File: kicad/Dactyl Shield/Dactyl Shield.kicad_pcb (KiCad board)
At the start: 4 copper layers, 99.4 x 77.4 mm, 122 parts, among them J201 JST, J202 Split, J203 Column, J204 Thumb, J205 External, J206 Row, J207 Display, J208 Vic, J209 ResA, J212 ResB, J301 JST, J302 Split, J303 Column, J304 Thumb, J305 External, J306 Row, J307 Display, J308 Vic, J309 ResA, J312 ResB, Q201 AO3400A, Q301 AO3400A, SW201 Battery, SW202 Reset, SW203 LED, SW301 Battery, SW302 Reset, SW303 LED, U201 SRV05-4, U202 Nice!Nano/2040, U301 SRV05-4, U302 Nice!Nano/2040

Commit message: refactor: cleanup schematic; external -> foot
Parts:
- J205, J305: value External -> Foot
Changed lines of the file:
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@@
 			)
 		)
-		(property "Value" "External"
-			(at 0.9 -2.1 90)
+		(property "Value" "Foot"
+			(at 0.25 -2.1 90)
 			(layer "F.SilkS")
 			(effects
@@
 		(fp_arc
 			(start 6.938123 15.132041)
-			(mid 6.337066 14.8831)
+			(mid 6.337062 14.8831)
 			(end 6.088123 14.282041)
 			(stroke
@@
 		(fp_arc
 			(start 8.236041 -15.740877)
-			(mid 8.837089 -15.491924)
+			(mid 8.837086 -15.491923)
 			(end 9.086041 -14.890877)
 			(stroke
@@
 		(fp_arc
 			(start 6.938123 15.132041)
-			(mid 6.337066 14.8831)
+			(mid 6.337062 14.8831)
 			(end 6.088123 14.282041)
 			(stroke
@@
 		(fp_arc
 			(start 8.236041 -15.740877)
-			(mid 8.837089 -15.491924)
+			(mid 8.837086 -15.491923)
 			(end 9.086041 -14.890877)
 			(stroke
@@
 			)
 		)
-		(property "Value" "External"
-			(at -0.9 -2 90)
+		(property "Value" "Foot"
+			(at -0.35 -2 90)
 			(layer "F.SilkS")
 			(effects

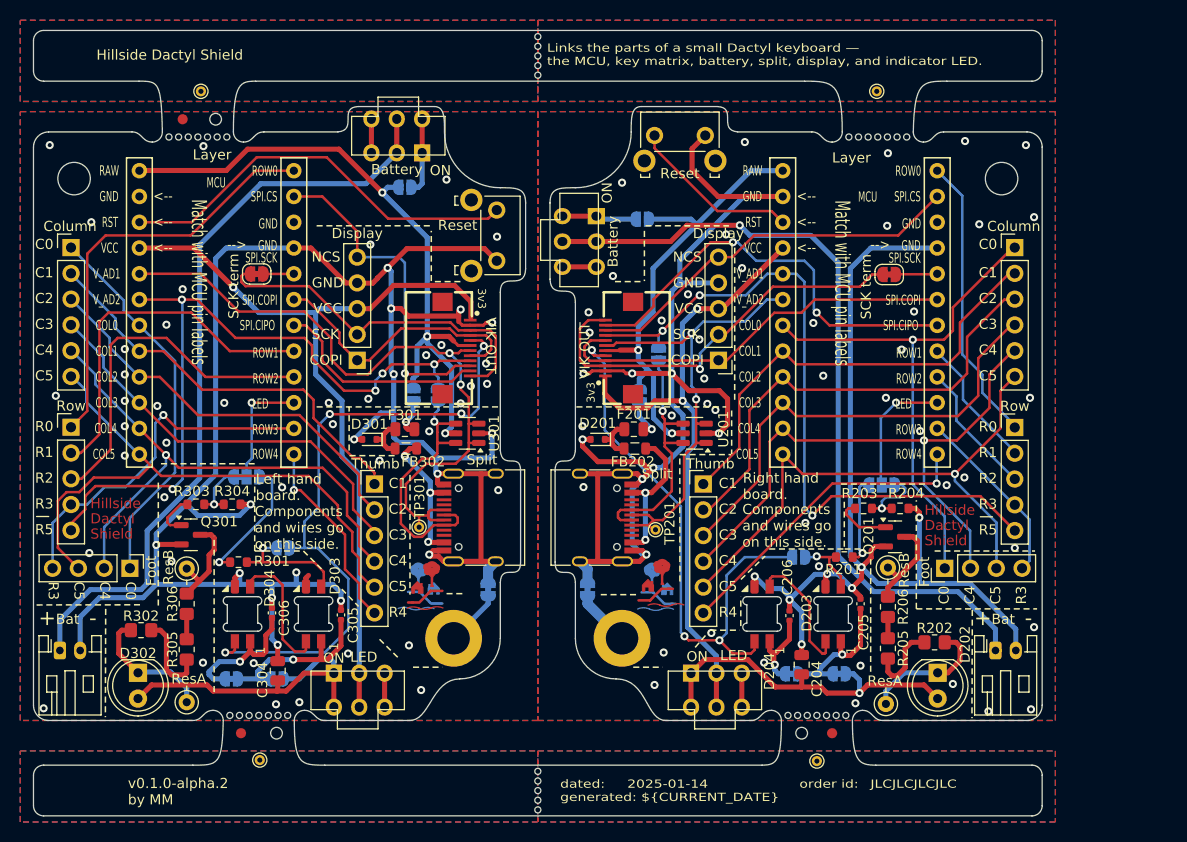
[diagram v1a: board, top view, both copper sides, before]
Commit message: feat: reset on back, power slides to right
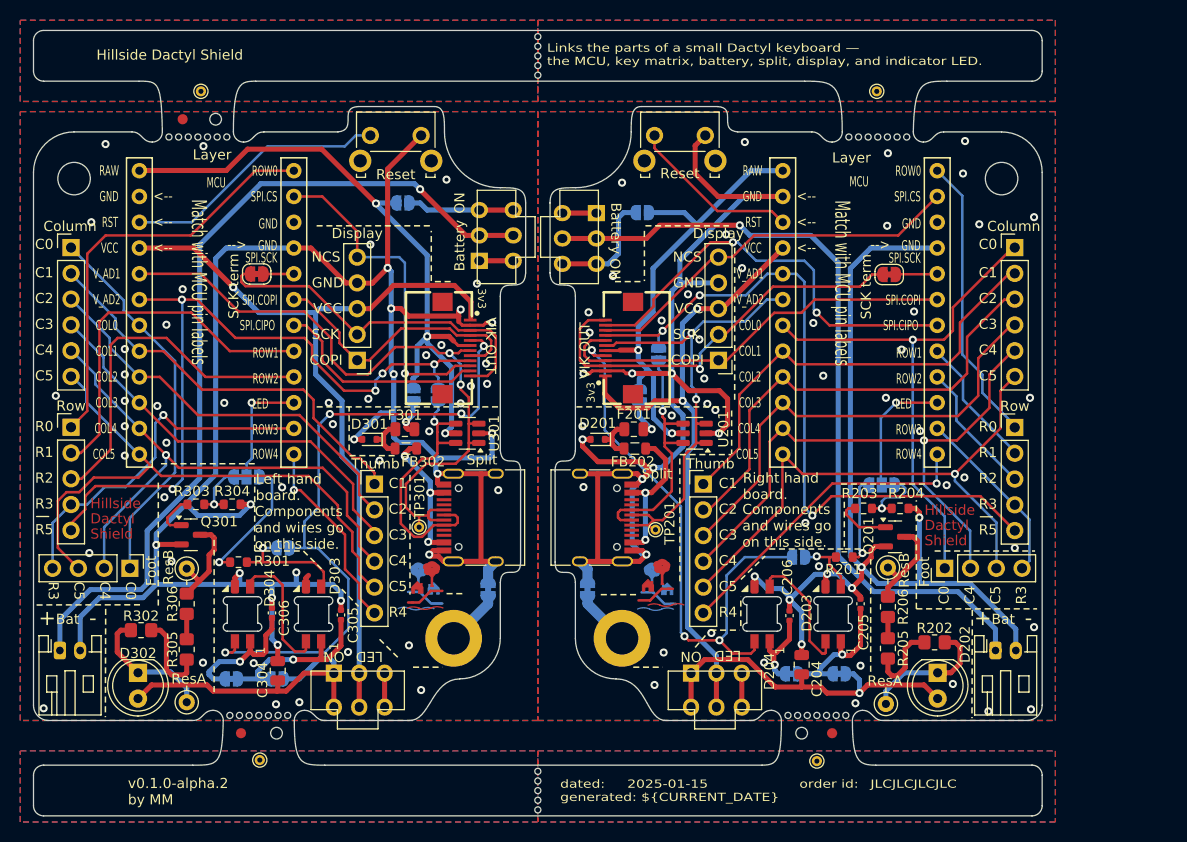
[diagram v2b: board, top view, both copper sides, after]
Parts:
- moved SW301 13.9 mm to (135.4, 85.2), turned to 90 degrees
- moved SW302 12.2 mm to (125.5, 76.6), turned to 180 degrees
- moved JP301 1.56 mm to (126.2, 82.0)
- moved JP201 0.65 mm to (149.8, 83.0)
- moved SW201 0.30 mm to (143.6, 85.5)
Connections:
- SW201 pad 1: /Right/POWER_BAT -> unconnected-(SW201-A-Pad1)_2
- SW201 pad 3: unconnected-(SW201-C-Pad3) -> /Right/POWER_BAT
- SW301 pad 1: /Left/POWER_BAT -> unconnected-(SW301-A-Pad1)_2
- SW301 pad 3: unconnected-(SW301-C-Pad3)_2 -> /Left/POWER_BAT
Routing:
- net /Left/RST: track 40.7 -> 26.3 mm
- net /Left/bat+: track 71.8 -> 80.9 mm, vias 0 -> 1
- net /Right/POWER_BAT: track 4.00 -> 8.12 mm
- net /Left/POWER_BAT: track 4.22 -> 7.17 mm
- net /Left/GND: track 200.1 -> 202.5 mm
- net /Left/RAW: track 66.5 -> 65.7 mm
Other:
- outline, holes or cut-outs redrawn

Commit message: feat: use open solder jumpers to LEDs
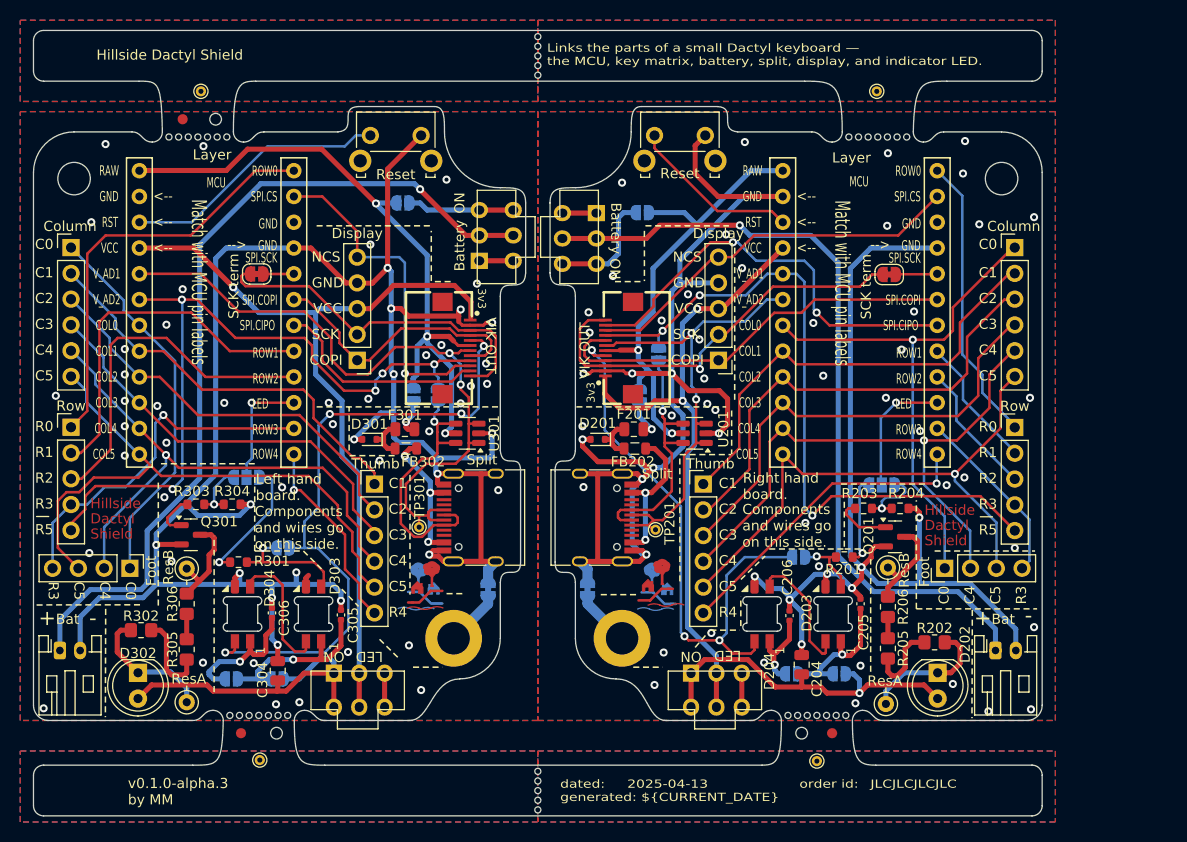
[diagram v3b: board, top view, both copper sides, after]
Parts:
- removed JP308: LED_Data, Jumper:SolderJumper-3_P1.3mm_Bridged12_RoundedPad1.0x1.5mm
- added JP310: LED_DATA, Jumper:SolderJumper-3_P1.3mm_Open_RoundedPad1.0x1.5mm, B.Cu at (110.8, 109.0)
- JP205, JP209, JP305, JP309: footprint Dactyl_basics:SolderJumper-2_P1.3mm_Bridged_RoundedPad1.0x1.5mm -> Dactyl_basics:SolderJumper-2_P1.3mm_Open_RoundedPad1.0x1.5mm
- JP208: value LED_Data -> LED_DATA; footprint Jumper:SolderJumper-3_P1.3mm_Bridged12_RoundedPad1.0x1.5mm -> Jumper:SolderJumper-3_P1.3mm_Open_RoundedPad1.0x1.5mm

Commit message: feat: reduce ground pin connections for thermal
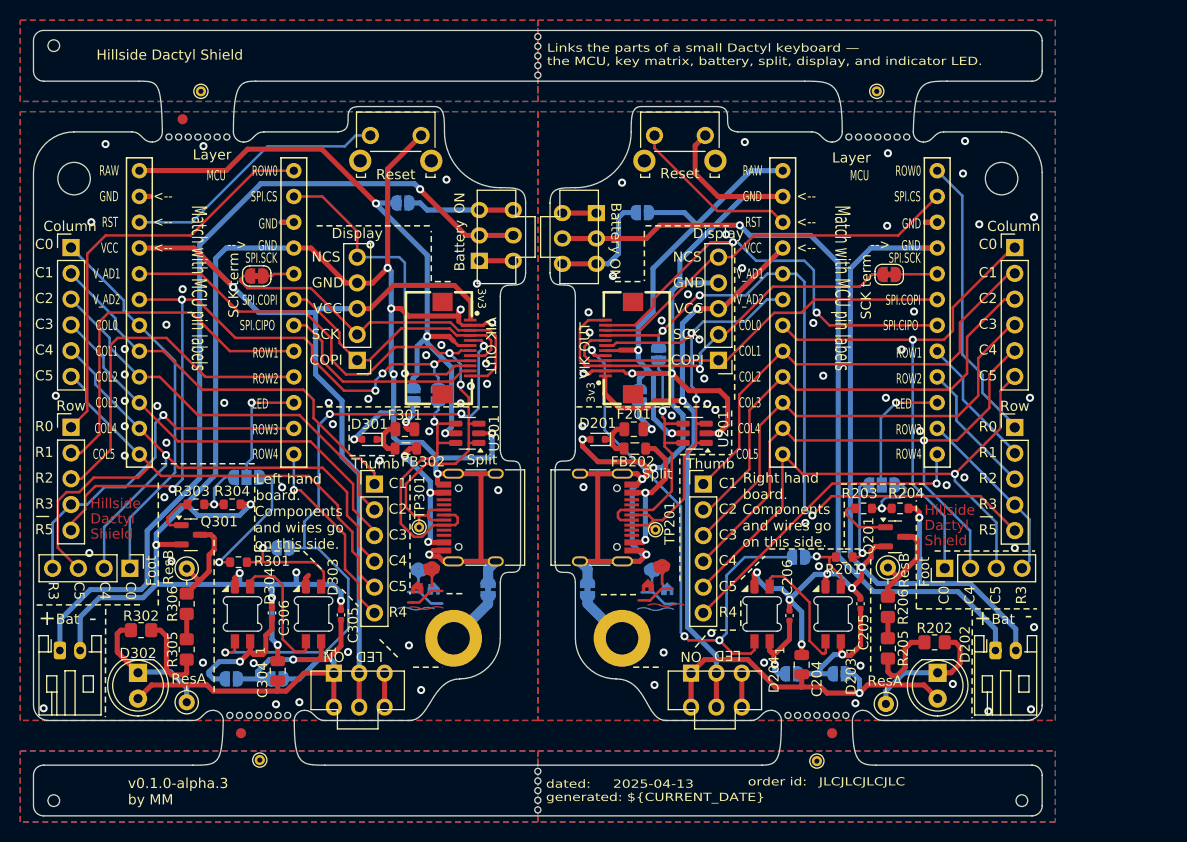
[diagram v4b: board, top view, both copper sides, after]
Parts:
- moved H102 22.9 mm to (91.8, 140.9)
- moved H103 22.7 mm to (187.2, 140.9)
- moved H101 17.5 mm to (91.8, 66.5)
- moved JP303 0.20 mm to (111.8, 89.2)
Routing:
- net /Left/GND: track 202.5 -> 224.4 mm
- net /Right/GND: track 216.9 -> 237.6 mm
